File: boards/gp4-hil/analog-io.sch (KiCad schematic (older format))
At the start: 107 parts, among them U10 AD9609, U11 DAC084S085, U12 DAC084S085, U13 DAC084S085, U14 DAC084S085, U2 XC7A100T-1FTG256C, U8 ADG726, U9 AD9609

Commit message: Added lots of analog I/O stuff
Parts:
- added C145, C146, C149, C150, C151, C152, C153, C154: 0.1 uF, symbol C
- added C147, C148: 1 uF, symbol C
- added C155, C156, C157, C158, C159, C160, C161, C162: 0.47 uF, symbol C
- added R138, R139: 10K 1%, symbol R
- added R140, R141: 100, symbol R
- added U19, U25, U26, U27, U28: TS3A4751, symbol TS3A4751
- R38, R39, R40, R41, R42, R43, R44, R45, R46, R47, R48, R49, R50, R51, R52, R53, R54, R55, R56, R57, R58: value 5K 0.5% -> 2.49k 0.1%
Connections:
- net A3V3: now also U11.7 (VREFIN), U12.7 (VREFIN), U13.7 (VREFIN), U14.7 (VREFIN), C155.1, C156.1, C157.1, C158.1, C159.1, C160.1, C161.1, C162.1, U25.14 (VCC), U26.14 (VCC), U27.14 (VCC), U28.14 (VCC)
- net ADC_A_CLK_N: now also C154.2; no longer U2.G12 (IO_L19N_T3_A21_VREF_15)
- net ADC_A_CLK_P: now also C153.2; no longer U2.H11 (IO_L19P_T3_A22_15)
- net ADC_B_CLK_N: now also C152.2; no longer U2.C16 (IO_L10P_T1_AD11P_15)
- net ADC_B_CLK_P: now also C151.2; no longer U2.A15 (IO_L9N_T1_DQS_AD3N_15)
- net ADC_CS_N: now also U2.A15 (IO_L9N_T1_DQS_AD3N_15); no longer U2.B16 (IO_L10N_T1_AD11N_15)
- net DAC_A_DIN: no longer U13.8 (DIN)
- net DAC_B_DIN: no longer U14.8 (DIN)
- net DAC_C_DIN: now also U13.8 (DIN)
- net DAC_D_DIN: now also U14.8 (DIN)
- net DUT_GPIO10: now also U25.11 (NO4)
- net DUT_GPIO12: now also U27.1 (NO1)
- net DUT_GPIO13: now also U26.3 (NO2)
- net DUT_GPIO14: now also U26.8 (NO3)
- net DUT_GPIO15: now also U26.11 (NO4)
- net DUT_GPIO17: now also U28.1 (NO1)
- net DUT_GPIO3: now also U25.1 (NO1)
- net DUT_GPIO4: now also U19.3 (NO2)
- net DUT_GPIO5: now also U19.8 (NO3)
- net DUT_GPIO6: now also U19.11 (NO4)
- net DUT_GPIO7: now also U26.1 (NO1)
- net DUT_GPIO8: now also U25.3 (NO2)
- net DUT_GPIO9: now also U25.8 (NO3)
- net GND: now also U10.26 (SENSE), U9.26 (SENSE), C145.2, C146.2, C147.2, C148.2, C149.2, C150.2, C155.2, C156.2, C157.2, C158.2, R138.2, R139.2, U25.7 (GND), U26.7 (GND), U27.7 (GND), U28.7 (GND)
- net GPIO10_ASIG: now also U25.10 (COM4)
- net GPIO12_ASIG: now also U27.2 (COM1)
- net GPIO13_ASIG: now also U26.4 (COM2)
- net GPIO14_ASIG: now also U26.9 (COM3)
- net GPIO15_ASIG: now also U26.10 (COM4)
- net GPIO17_ASIG: now also U28.2 (COM1)
- net GPIO3_ASIG: now also U25.2 (COM1)
- net GPIO4_ASIG: now also U19.4 (COM2)
- net GPIO5_ASIG: now also U19.9 (COM3)
- net GPIO6_ASIG: now also U19.10 (COM4)
- net GPIO7_ASIG: now also U26.2 (COM1)
- net GPIO8_ASIG: now also U25.4 (COM2)
- net GPIO9_ASIG: now also U25.9 (COM3)
- net ADC_B_MODE: now reaches U2.H14 (IO_L24P_T3_RS1_15)
- net ADC_B_MODE: now also U10.23 (MODE/OR)
- net ADC_A_MODE: now reaches U2.J16 (IO_L23N_T3_FWE_B_15)
- net ADC_A_MODE: now also U9.23 (MODE/OR)
- net ADC1_VREF: now reaches U9.25 (VREF)
- net ADC1_VREF: now also C145.1, C147.1
- net ADC1_VCM: now reaches U9.27 (VCM)
- net ADC1_VCM: now also C149.1
- net at U9.28 (RBIAS): now also R138.1
- net ADC2_VREF: now reaches U10.25 (VREF)
- net ADC2_VREF: now also C146.1, C148.1
- net ADC2_VCM: now reaches U10.27 (VCM)
- net ADC2_VCM: now also C150.1
- net at U10.28 (RBIAS): now also R139.1
- new net: C152.1, R140.2, U2.B16 (IO_L10N_T1_AD11N_15)
- new net: C151.1, R140.1, U2.C16 (IO_L10P_T1_AD11P_15)
- new net: C154.1, R141.2, U2.G12 (IO_L19N_T3_A21_VREF_15)
- new net: C153.1, R141.1, U2.H11 (IO_L19P_T3_A22_15)
- new net GPIO10_AEN: U25.12 (IN4)
- new net GPIO12_AEN: U27.13 (IN1)
- new net GPIO13_AEN: U26.5 (IN2)
- new net GPIO14_AEN: U26.6 (IN3)
- new net GPIO15_AEN: U26.12 (IN4)
- new net GPIO17_AEN: U28.13 (IN1)
- new net GPIO3_AEN: U25.13 (IN1)
- new net GPIO4_AEN: U19.5 (IN2)
- new net GPIO5_AEN: U19.6 (IN3)
- new net GPIO6_AEN: U19.12 (IN4)
- new net GPIO7_AEN: U26.13 (IN1)
- new net GPIO8_AEN: U25.5 (IN2)
- new net GPIO9_AEN: U25.6 (IN3)
- no-connect marks 19 -> 17
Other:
- note added: "1v p-p analog input, 10 bits:\n* 4V max (attenuation of 4): 3.9 mV resolution\n* 8V max (attenuation of 8): 7.8 mV resolution\n\nWith 5k ohm split attenuator from Vin to signal,\nwe waste ~~1 mW in leakage per attenuator"
- note added: "TODO: Can we do LVDS at VCCO=2.5?"
- note added: "VCCO=2V5"
- note removed: "2v p-p analog input, 10 bits:\n* 4V max (attenuation of 2): 3.9 mV resolution\n* 8V max (attenuation of 4): 7.8 mV resolution\n\nWith 5k ohm split attenuator from Vin to signal,\nwe waste ~~1 mW in leakage per attenuator"
- moved on the sheet: C46, C47, C48, C49, C50, C51, C52, C53

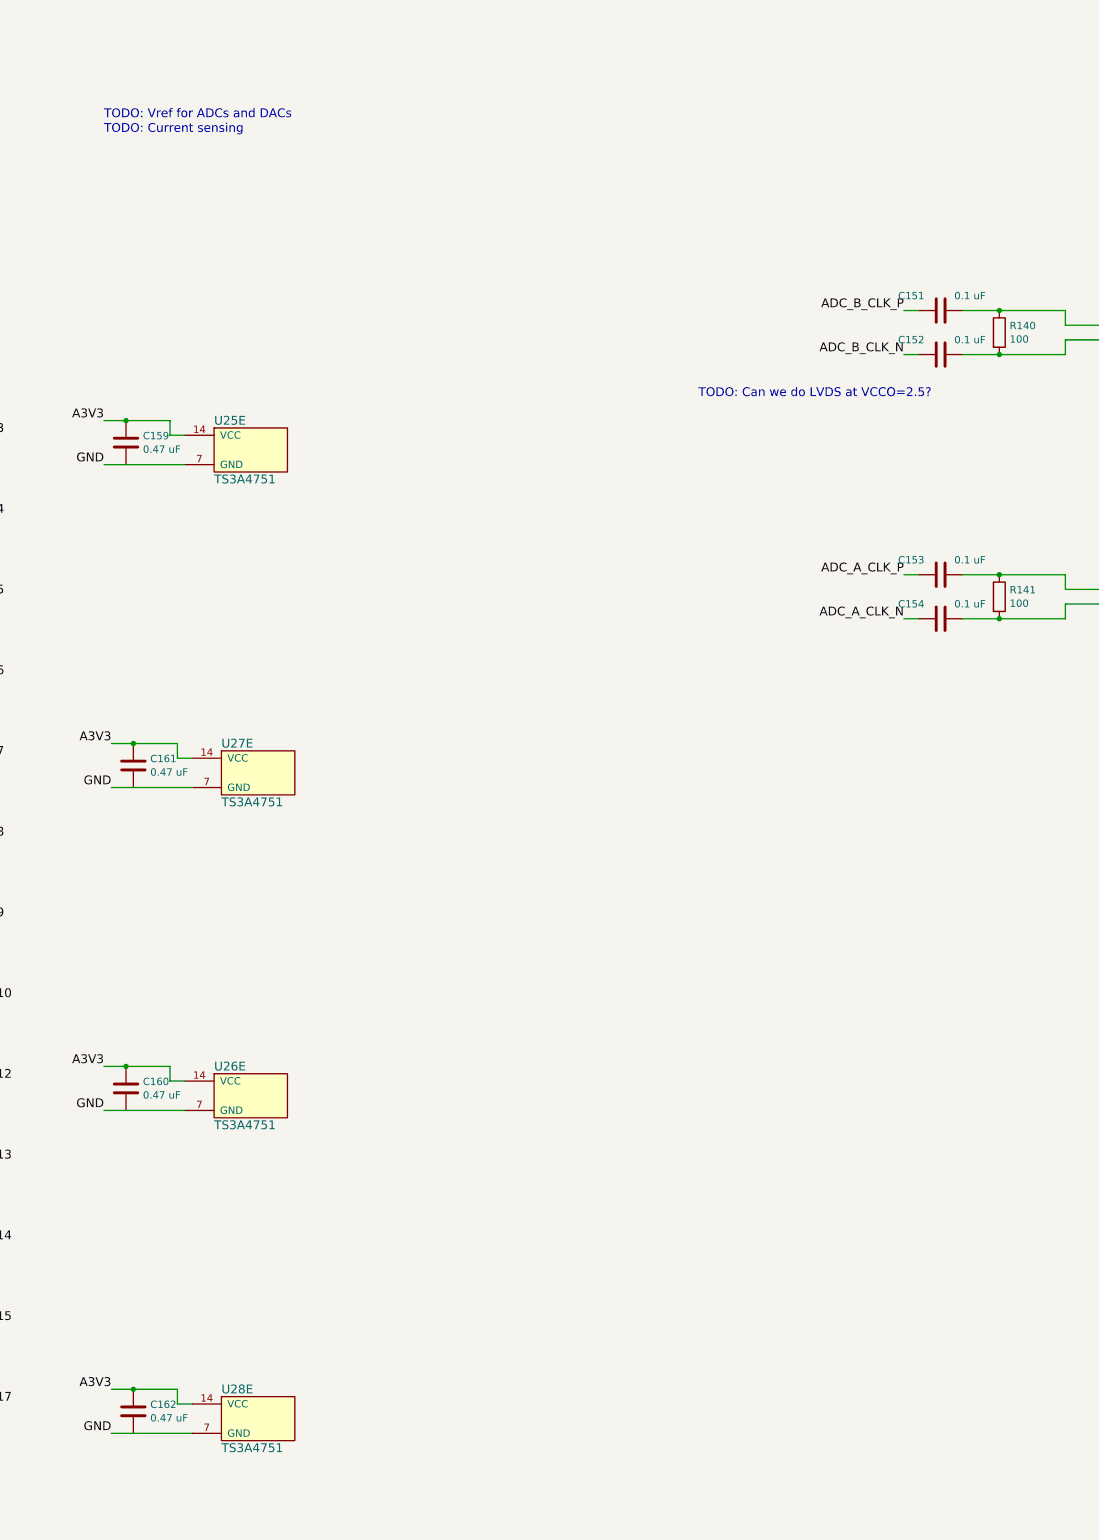
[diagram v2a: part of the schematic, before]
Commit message: Continued schematic capture, added JTAG master interfaces
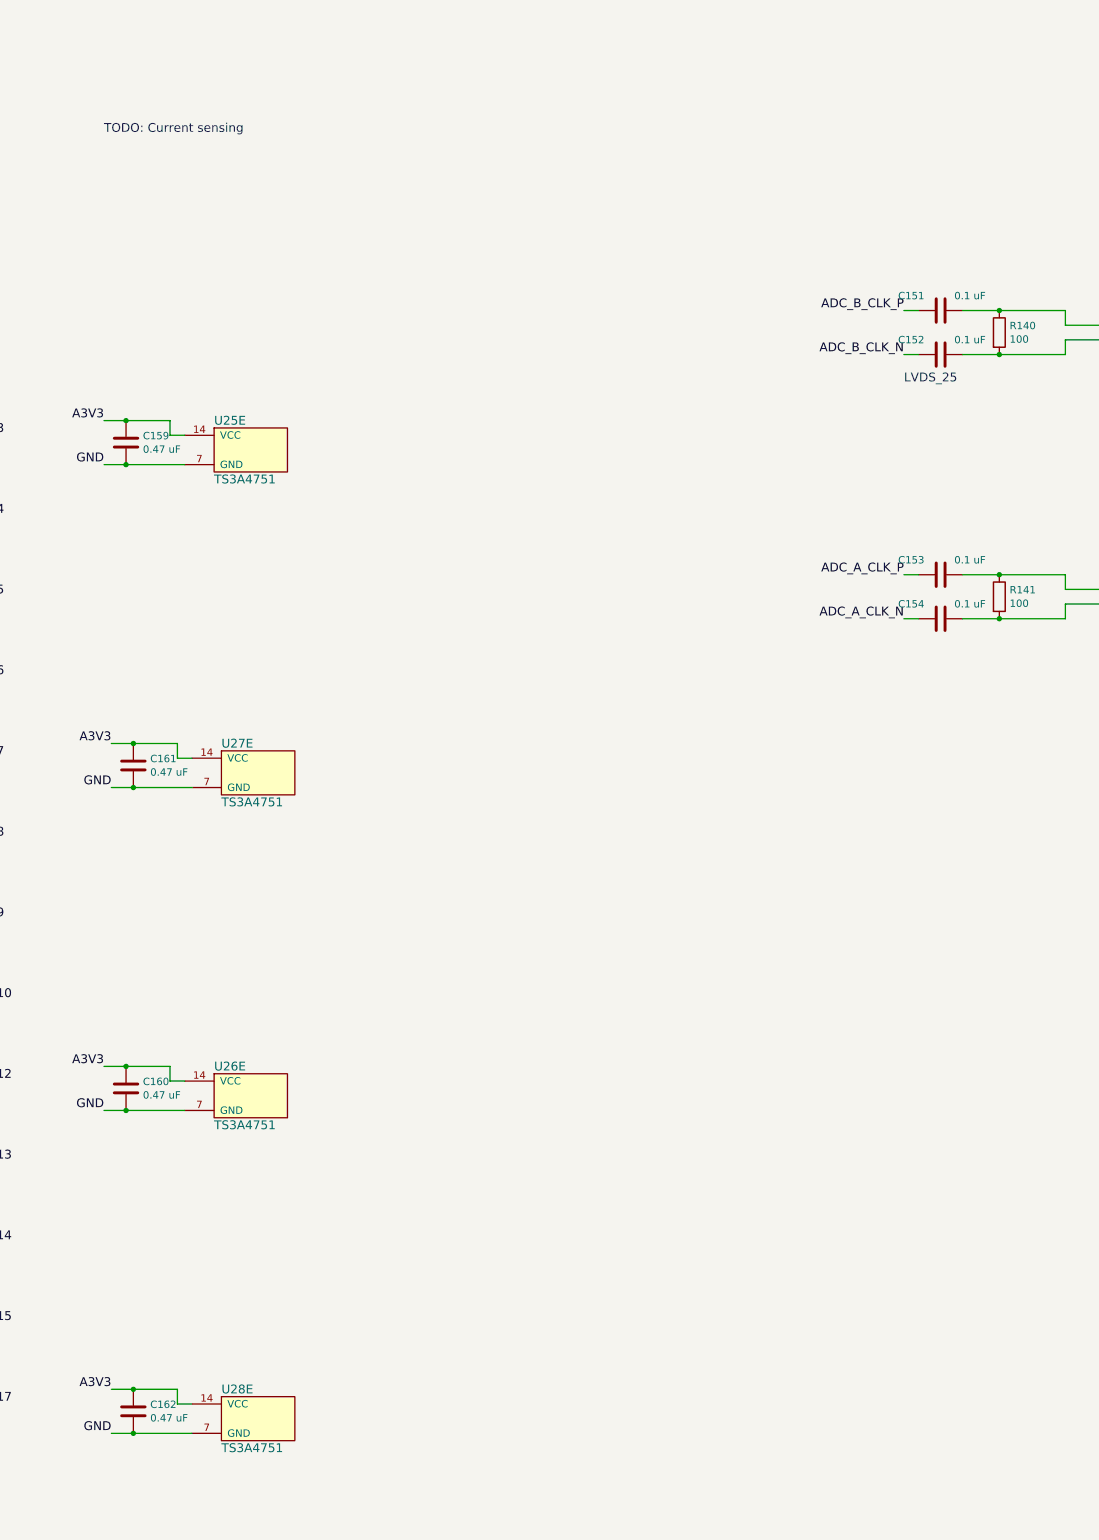
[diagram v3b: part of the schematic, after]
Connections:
- net GND: now also C159.2, C160.2, C161.2, C162.2
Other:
- note added: "LVDS_25"
- note removed: "TODO: Can we do LVDS at VCCO=2.5?"
- note removed: "TODO: Vref for ADCs and DACs"
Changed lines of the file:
@@
 Text Label 1450 8700 2    60   ~ 0
 A1V8
-Text Notes 13200 1650 0    60   ~ 0
-TODO: Vref for ADCs and DACs
 Text Label 1450 10500 2    60   ~ 0
 ADC_CS_N
@@
 Wire Wire Line
 	19750 4750 19750 4850
-Text Notes 17250 3550 0    60   ~ 0
-TODO: Can we do LVDS at VCCO=2.5?
 Wire Wire Line
 	18650 2950 18750 2950
@@
 Text Label 13200 4000 2    60   ~ 0
 GND
-Wire Wire Line
-	13200 4000 13750 4000
 $Comp
 L C C159
@@
 Text Label 13250 6200 2    60   ~ 0
 GND
-Wire Wire Line
-	13250 6200 13800 6200
 $Comp
 L C C161
@@
 Text Label 13200 8400 2    60   ~ 0
 GND
-Wire Wire Line
-	13200 8400 13750 8400
 $Comp
 L C C160
@@
 Text Label 13250 10600 2    60   ~ 0
 GND
-Wire Wire Line
-	13250 10600 13800 10600
 $Comp
 L C C162
@@
 	13700 10400 13800 10400
 Connection ~ 13400 10300
+Wire Wire Line
+	13200 4000 13750 4000
+Connection ~ 13350 4000
+Wire Wire Line
+	13250 6200 13800 6200
+Connection ~ 13400 6200
+Wire Wire Line
+	13200 8400 13750 8400
+Connection ~ 13350 8400
+Wire Wire Line
+	13250 10600 13800 10600
+Connection ~ 13400 10600
+Text Notes 18650 3450 0    60   ~ 0
+LVDS_25
 $EndSCHEMATC

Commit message: Added ADC driver. ERC-clean except for paralleled LTC3374 output channels. Still needs indicator LEDs and core clock for the FPGA, plus lots of test points etc
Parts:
- added C167, C168: 0.47 uF, symbol C
- added C169, C170: 4.7 uF, symbol C
- added R142, R143, R144, R145, R146, R147, R148, R149: 100K 0.1%, symbol R
- added U31: ADA4937-2, symbol ADA4937-2
- R17: value 15K 0.5% -> 30K 0.1%
- R18: value 5K 0.5% -> 71.5K 0.1%
- R19, R20, R21, R22, R23, R24, R25, R26, R27, R28, R29, R30, R31, R32, R33, R34, R35, R36, R37: value 5K 0.5% -> 30K 0.1%
- R38, R39, R40, R41, R42, R43, R44, R45, R46, R47, R48, R49, R50, R51, R52, R53, R54, R55, R56, R57, R58: value 2.49k 0.1% -> 10K 0.1%
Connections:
- net A3V3: now also C167.2, C168.2, C169.2, C170.2, U31.10 (VDD), U31.14 (PD_N), U31.20 (PD_N), U31.3 (VDD), U31.4 (VDD), U31.9 (VDD)
- net ADC_A_VIN: now also R142.2
- net ADC_B_VIN: now also R144.2
- net ADC_IN0: now also R18.1; no longer R17.1
- net ADC_IN1: now also R17.1; no longer R18.1
- net DUT_VDD1: now also R17.2; no longer R18.2
- net DUT_VPP: now also R18.2; no longer R17.2
- net GND: now also C167.1, C168.1, C169.1, C170.1, R143.2, R145.2, U31.15 (VSS), U31.16 (VSS), U31.21 (VSS), U31.22 (VSS)
- net ADC_A_N: now reaches U9.30 (VIN_N)
- net ADC_A_N: now also U31.19 (OUT_N)
- net ADC_A_P: now reaches U9.31 (VIN_P)
- net ADC_A_P: now also U31.18 (OUT_P)
- net ADC_B_N: now reaches U10.30 (VIN_N)
- net ADC_B_N: now also U31.13 (OUT_N)
- net ADC_B_P: now reaches U10.31 (VIN_P)
- net ADC_B_P: now also U31.12 (OUT_P)
- net ADC1_VCM renamed ADC_A_VCM
- net ADC_A_VCM: now also U31.17 (VOCM)
- net ADC1_VREF renamed ADC_A_VREF
- net ADC2_VCM renamed ADC_B_VCM
- net ADC_B_VCM: now also U31.11 (VOCM)
- net ADC2_VREF renamed ADC_B_VREF
- new net: R143.1, R147.2, U31.1 (IN_N)
- new net: R147.1, U31.2 (FB_P)
- new net: R146.1, U31.23 (FB_N)
- new net: R142.1, R146.2, U31.24 (IN_P)
- new net: R148.1, U31.5 (FB_N)
- new net: R144.1, R148.2, U31.6 (IN_P)
- new net: R145.1, R149.2, U31.7 (IN_N)
- new net: R149.1, U31.8 (FB_P)
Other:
- note removed: "TODO:\n* How to couple clock inputs? Diff term?\n* How to couple inputs from mux?"

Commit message: Added FPGA core clock, GPIO indicator LEDs, expansion header, lots of test points
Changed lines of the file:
@@
 Text HLabel 1300 800  0    60   Input ~ 0
 DUT_VDD1
-Text HLabel 1300 900  0    60   Input ~ 0
-DUT_VDD2
 Text HLabel 1500 3950 0    60   Input ~ 0
 GND
@@
 Text Label 2200 2600 0    60   ~ 0
 ADC_IN18
-Text Label 2200 2700 0    60   ~ 0
-ADC_IN19
 Text Label 1500 3750 2    60   ~ 0
 A2V5
@@
 Text Label 3150 6050 0    60   ~ 0
 ADC_IN18
-Text Label 3150 6150 0    60   ~ 0
-ADC_IN19
 $Comp
 L C C27
@@
 	1800 700  2900 700
 Wire Wire Line
-	1500 700  1300 700
-Wire Wire Line
 	3650 700  3200 700
 Wire Wire Line
@@
 	1500 2600 1300 2600
 Wire Wire Line
-	1800 2700 2900 2700
-Wire Wire Line
-	1500 2700 1300 2700
-Wire Wire Line
 	3650 700  3650 2700
 Connection ~ 3650 800
@@
 Connection ~ 3650 2400
 Connection ~ 3650 2500
-Connection ~ 3650 2600
 Wire Wire Line
 	1550 4250 1650 4250
@@
 	3050 6050 3150 6050
 Wire Wire Line
-	3150 6150 3050 6150
+	3150 6250 3050 6250
 Wire Wire Line
 	1700 7550 2950 7550
@@
 PSU_VTEMP
 Wire Wire Line
-	3150 6250 3050 6250
-Wire Wire Line
 	3650 800  3200 800
 Wire Wire Line
@@
 Wire Wire Line
 	3650 2600 3200 2600
-Wire Wire Line
-	3650 2700 3200 2700
 $Comp
 L C C145
@@
 	19750 4950 20650 4950
 Wire Wire Line
-	19750 4950 19750 5050
+	19750 5050 19750 4950
 Wire Wire Line
 	19750 4750 19750 4850
@@
 $EndComp
 Wire Wire Line
-	19750 5050 19050 5050
+	19050 5050 19750 5050
 Wire Wire Line
 	19050 4750 19750 4750
@@
 $EndComp
 $Comp
-L R R37
-U 1 1 5750E582
-P 1650 2700
-F 0 "R37" V 1600 2450 50  0000 C CNN
-F 1 "30K 0.1%" V 1600 3000 50  0000 C CNN
-F 2 "" V 1580 2700 30  0000 C CNN
-F 3 "" H 1650 2700 30  0000 C CNN
-	1    1650 2700
-	0    1    1    0
-$EndComp
-$Comp
 L R R39
 U 1 1 5750E782
@@
 $EndComp
 $Comp
-L R R58
-U 1 1 5750FA7F
-P 3050 2700
-F 0 "R58" V 3000 2450 50  0000 C CNN
-F 1 "10K 0.1%" V 3000 3000 50  0000 C CNN
-F 2 "" V 2980 2700 30  0000 C CNN
-F 3 "" H 3050 2700 30  0000 C CNN
-	1    3050 2700
-	0    1    1    0
-$EndComp
-$Comp
 L R R38
 U 1 1 5750FC3F
@@
 Wire Wire Line
 	8900 14450 9250 14450
+Text HLabel 1300 900  0    60   Input ~ 0
+DUT_VDD2
+Text Label 2200 2700 0    60   ~ 0
+ADC_IN19
+Wire Wire Line
+	1800 2700 2900 2700
+Wire Wire Line
+	1500 2700 1300 2700
+Wire Wire Line
+	3650 2700 3200 2700
+$Comp
+L R R37
+U 1 1 57542996
+P 1650 2700
+F 0 "R37" V 1600 2450 50  0000 C CNN
+F 1 "30K 0.1%" V 1600 3000 50  0000 C CNN
+F 2 "" V 1580 2700 30  0000 C CNN
+F 3 "" H 1650 2700 30  0000 C CNN
+	1    1650 2700
+	0    1    1    0
+$EndComp
+$Comp
+L R R58
+U 1 1 5754299C
+P 3050 2700
+F 0 "R58" V 3000 2450 50  0000 C CNN
+F 1 "10K 0.1%" V 3000 3000 50  0000 C CNN
+F 2 "" V 2980 2700 30  0000 C CNN
+F 3 "" H 3050 2700 30  0000 C CNN
+	1    3050 2700
+	0    1    1    0
+$EndComp
+Connection ~ 3650 2600
+Text Label 3150 6150 0    60   ~ 0
+ADC_IN19
+Wire Wire Line
+	3150 6150 3050 6150
+Wire Wire Line
+	1300 700  1500 700
 $EndSCHEMATC
